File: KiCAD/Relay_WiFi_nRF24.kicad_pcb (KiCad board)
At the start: 2 copper layers, 50.8 x 50.8 mm, 15 parts, among them IC1 MOC3061M, P1 CONN_4, P2 CONN_4, P3 CONN_01X04, U1 ESP8266-ESP-03, U2 NCP1117ST33T3G, U3 NRF24L01P_SMD, U4 TRIAC

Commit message: Мелкие изменения
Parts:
- moved C2 1.27 mm to (171.4, 133.3)
- moved P2 0.57 mm to (170.2, 152.4)
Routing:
- net Net-(C2-Pad2): track 68.4 -> 75.0 mm
- net Net-(C2-Pad1): track 9.78 -> 10.5 mm

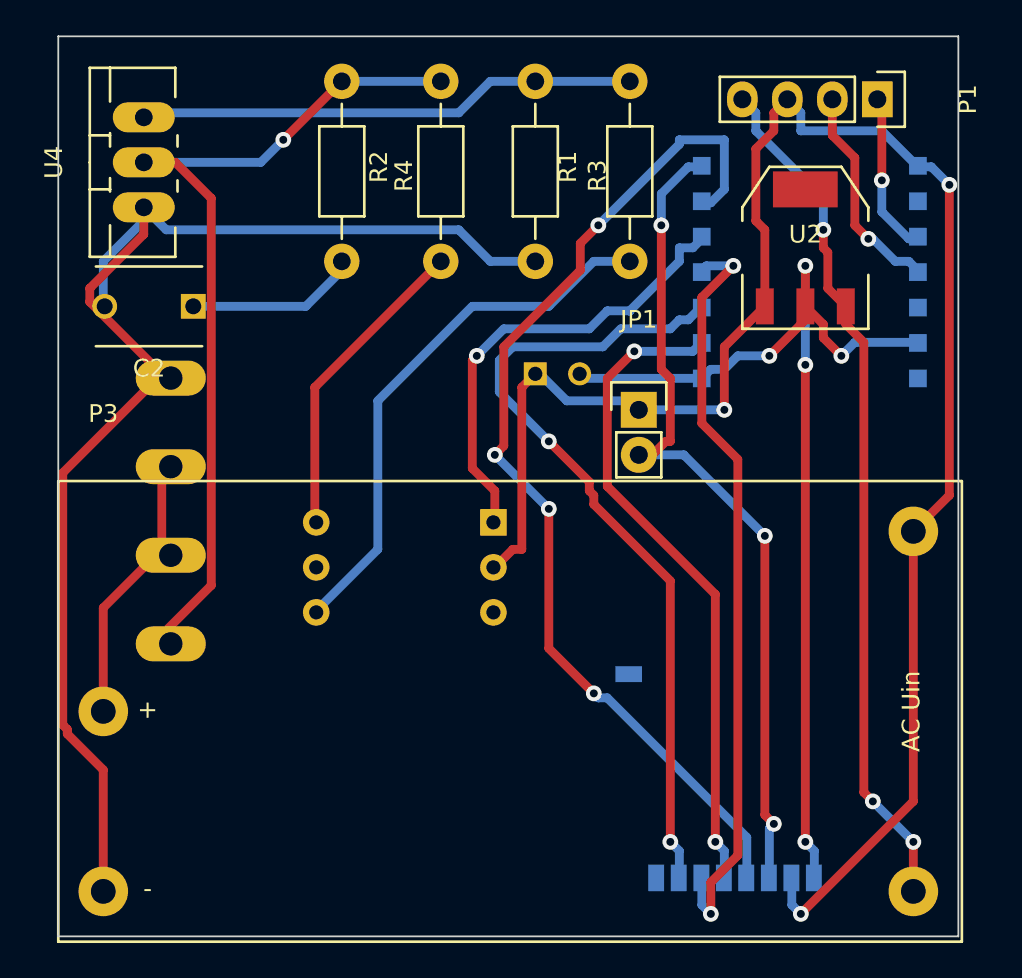
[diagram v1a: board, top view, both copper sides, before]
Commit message: Изменение прототипа платы
Развернул радиомодули, переложил дорожки, увеличил ширину дорожек
силовой части
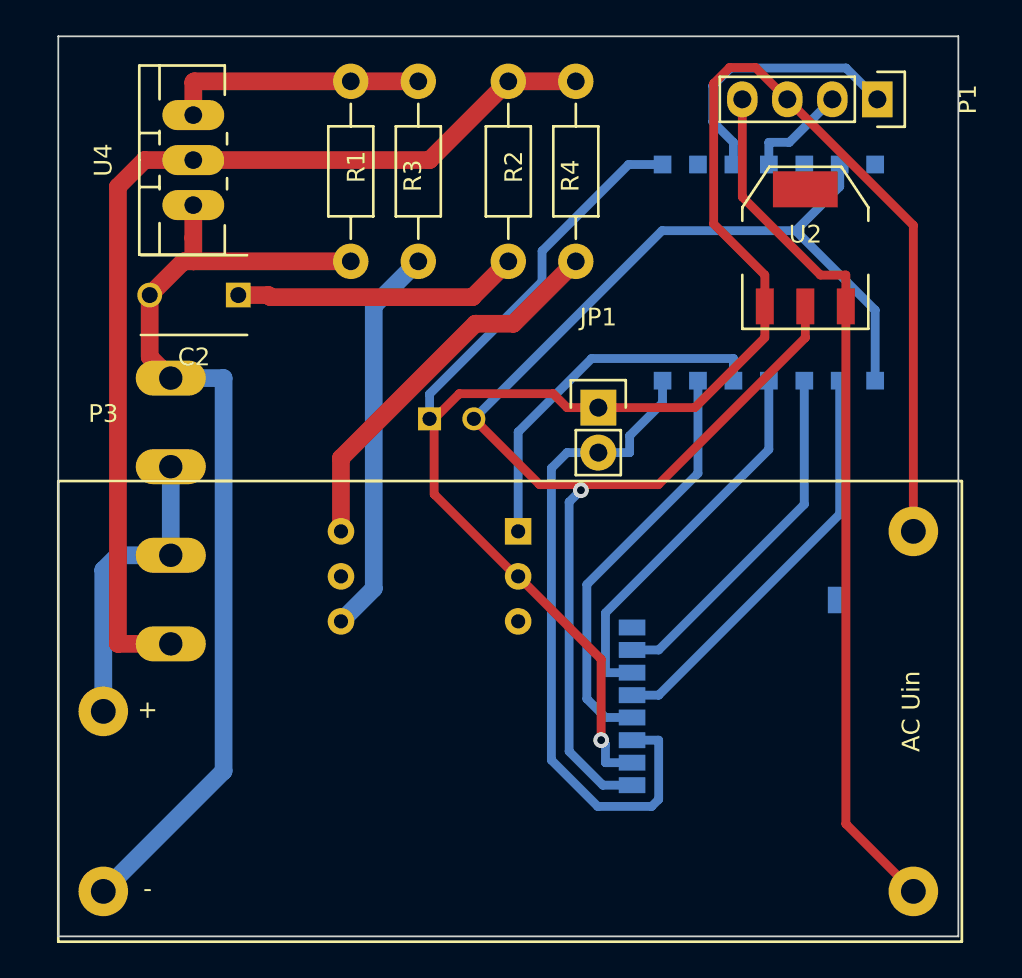
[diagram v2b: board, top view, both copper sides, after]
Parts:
- moved U3 12.4 mm to (196.2, 161.9), turned to 0 degrees
- moved R1 11.9 mm to (184.2, 125.7)
- moved R3 10.4 mm to (180.3, 125.7)
- moved R4 9.40 mm to (189.2, 125.7)
- moved R2 7.62 mm to (193.0, 125.7)
- moved C1 6.49 mm to (184.8, 139.7)
- moved U4 2.80 mm to (171.4, 125.1)
- moved C2 2.62 mm to (174.0, 132.7)
- moved U1 2.42 mm to (203.8, 131.4), turned to 90 degrees
- moved JP1 2.29 mm to (194.3, 139.1)
- moved IC1 1.49 mm to (184.8, 148.6)
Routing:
- net Net-(U1-Pad13): track 59.2 -> 23.5 mm, vias 4 -> 0
- net Net-(U1-Pad10): track 46.2 -> 20.1 mm, vias 2 -> 0
- net Net-(C1-Pad2): track 60.4 -> 82.8 mm, vias 5 -> 1
- net Net-(U1-Pad11): track 43.0 -> 21.8 mm, vias 2 -> 0
- net Net-(C2-Pad2): track 75.0 -> 55.3 mm
- net Net-(R1-Pad2): track 28.3 -> 14.6 mm
- net Net-(U1-Pad9): track 37.2 -> 23.5 mm, vias 2 -> 0
- net GND: track 101.9 -> 115.5 mm, vias 3 -> 1
- net Net-(JP1-Pad2): track 47.9 -> 38.2 mm, vias 3 -> 0
- net Net-(IC1-Pad4): track 31.0 -> 22.1 mm
- net Net-(P2-Pad1): track 49.4 -> 57.1 mm, vias 1 -> 0
- net Net-(P1-Pad2): track 12.3 -> 5.84 mm, vias 1 -> 0
- net Net-(P1-Pad1): track 9.24 -> 15.4 mm, vias 1 -> 0
- net Net-(C2-Pad1): track 10.5 -> 16.1 mm
- net Net-(IC1-Pad1): track 26.1 -> 20.7 mm, vias 1 -> 0
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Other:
- net class Tolsto: via_dia 0.889 -> 1.3; via_drill 0.635 -> 1
